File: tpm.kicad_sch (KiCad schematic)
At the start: 3 parts, among them J21 PinHeader_2x7_P2mm_Drill0.9mm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

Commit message: Update naming on schematics, fix OSM page size
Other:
- title: BMC Reference Carrier Board -> DC-SCM Carrier Card for OSM-L SoMs
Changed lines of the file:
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@@
 	(paper "A3")
 	(title_block
-		(title "BMC Reference Carrier Board")
-		(date "2025-10-13")
+		(title "DC-SCM Carrier Card for OSM-L SoMs")
+		(date "2025-10-14")
 		(rev "1.1.0")
 	)

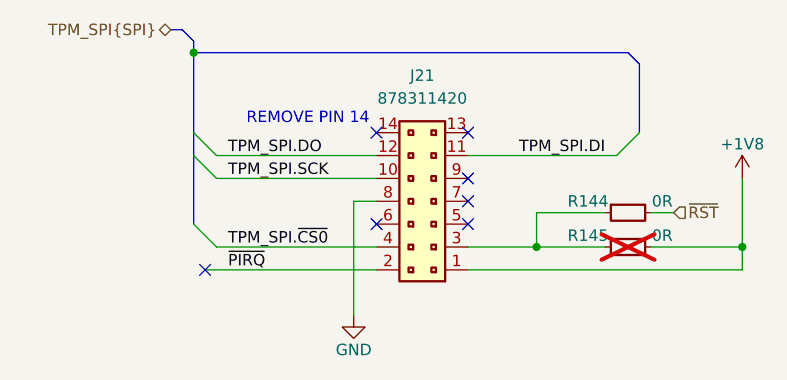
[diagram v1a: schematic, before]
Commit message: Change TPM connector
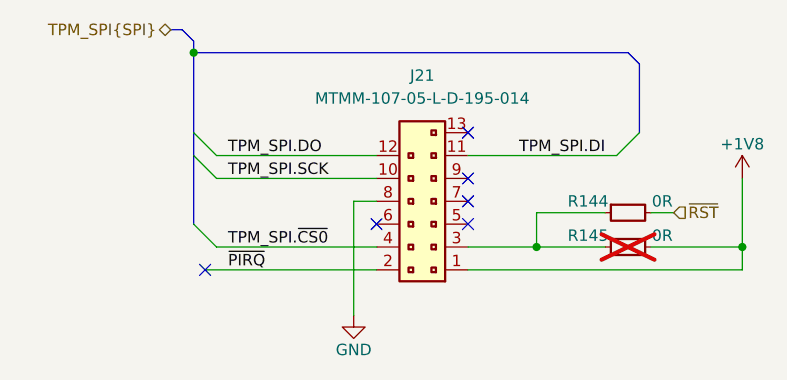
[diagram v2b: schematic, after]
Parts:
- removed J21: PinHeader_2x7_P2mm_Drill0.9mm_878311420, antmicro-footprints:PinHeader_2x7_P2mm_Drill0.9mm_878311420, symbol antmicroGenericPinHeaders:PinHeader_2x7_P2mm_Drill0.9mm_878311420
- added J21: PinHeader_2x7_P2mm_MTMM-107-05-L-D-195-014, antmicro-footprints:PinHeader_2x7_P2mm_Drill0.9mm_MTMM, symbol antmicroGenericPinHeaders:PinHeader_2x7_P2mm_MTMM-107-05-L-D-195-014
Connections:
- net +1V8: now also J21.1
- net GND: now also J21.8
- net TPM_SPI.DI: now also J21.11
- net TPM_SPI.DO: now also J21.12
- net TPM_SPI.SCK: now also J21.10
- net TPM_SPI.~{CS0}: now also J21.4
- net ~{PIRQ}: now also J21.2
- net at R144.1, R145.1: now also J21.3
- no-connect marks 7 -> 6
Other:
- note removed: "REMOVE PIN 14"
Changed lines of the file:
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@@
 		(rev "1.1.0")
-	)
-	(text "REMOVE PIN 14"
-		(exclude_from_sim no)
-		(at 199.39 134.366 0)
-		(effects
-			(font
-				(size 1.27 1.27)
-			)
-		)
 	)
 	(junction
@@
 	(no_connect
 		(at 187.96 151.13)
-	)
-	(no_connect
-		(at 207.01 135.89)
 	)
 	(no_connect
@@
 				)
 				(justify right)
+			)
+		)
+	)
+	(symbol
+		(lib_id "antmicroGenericPinHeaders:PinHeader_2x7_P2mm_MTMM-107-05-L-D-195-014")
+		(at 217.17 151.13 180)
+		(unit 1)
+		(exclude_from_sim no)
+		(in_bom yes)
+		(on_board yes)
+		(dnp no)
+		(fields_autoplaced yes)
+		(property "Reference" "J21"
+			(at 212.09 129.54 0)
+			(effects
+				(font
+					(size 1.27 1.27)
+					(thickness 0.15)
+				)
+			)
+		)
+		(property "Value" "PinHeader_2x7_P2mm_MTMM-107-05-L-D-195-014"
+			(at 191.77 140.97 0)
+			(effects
+				(font
+					(size 1.27 1.27)
+					(thickness 0.15)
+				)
+				(justify left bottom)
+				(hide yes)
+			)
+		)
+		(property "Footprint" "antmicro-footprints:PinHeader_2x7_P2mm_Drill0.9mm_MTMM"
+			(at 191.77 138.43 0)
+			(effects
+				(font
+					(size 1.27 1.27)
+					(thickness 0.15)
+				)
+				(justify left bottom)
+				(hide yes)
+			)
+		)
+		(property "Datasheet" "https://suddendocs.samtec.com/catalog_english/mtmm_th.pdf"
+			(at 191.77 135.89 0)
+			(effects
+				(font
+					(size 1.27 1.27)
+					(thickness 0.15)
+				)
+				(justify left bottom)
+				(hide yes)
+			)
+		)
+		(property "Description" "Pin Header, 2 Rows, 13 Contacts, 2.00mm"
+			(at 191.77 133.35 0)
+			(effects
+				(font
+					(size 1.27 1.27)
+					(thickness 0.15)
+				)
+				(justify left bottom)
+				(hide yes)
+			)
+		)
+		(property "MPN" "MTMM-107-05-L-D-195-014"
+			(at 212.09 132.08 0)
+			(effects
+				(font
+					(size 1.27 1.27)
+					(thickness 0.15)
+				)
+			)
+		)
+		(property "Manufacturer" "Samtec"
+			(at 191.77 130.81 0)
+			(effects
+				(font
+					(size 1.27 1.27)
+					(thickness 0.15)
+				)
+				(justify left bottom)
+				(hide yes)
+			)
+		)
+		(property "Author" "Antmicro"
+			(at 191.77 128.27 0)
+			(effects
+				(font
+					(size 1.27 1.27)
+					(thickness 0.15)
+				)
+				(justify left bottom)
+				(hide yes)
+			)
+		)
+		(property "License" "Apache-2.0"
+			(at 191.77 125.73 0)
+			(effects
+				(font
+					(size 1.27 1.27)
+					(thickness 0.15)
+				)
+				(justify left bottom)
+				(hide yes)
+			)
+		)
+		(pin "9"
+		)
+		(pin "7"
+		)
+		(pin "8"
+		)
+		(pin "2"
+		)
+		(pin "11"
+		)
+		(pin "1"
+		)
+		(pin "3"
+		)
+		(pin "13"
+		)
+		(pin "5"
+		)
+		(pin "12"
+		)
+		(pin "4"
+		)
+		(pin "6"
+		)
+		(pin "10"
+		)
+		(instances
+			(project ""
+				(path "/5f636c45-3c15-4731-8931-4625e0dab7e4/757bd70a-5179-4368-9172-3adb38876975"
+					(reference "J21")
+					(unit 1)
+				)
 			)
 		)
@@
 					(unit 1)
 				)
-			)
-		)
-	)
-	(symbol
-		(lib_id "antmicroGenericPinHeaders:PinHeader_2x7_P2mm_Drill0.9mm_878311420")
-		(at 217.17 151.13 180)
-		(unit 1)
-		(exclude_from_sim no)
-		(in_bom yes)
-		(on_board yes)
-		(dnp no)
-		(fields_autoplaced yes)
-		(property "Reference" "J21"
-			(at 212.09 129.54 0)
-			(effects
-				(font
-					(size 1.27 1.27)
-					(thickness 0.15)
-				)
-			)
-		)
-		(property "Value" "PinHeader_2x7_P2mm_Drill0.9mm_878311420"
-			(at 191.77 146.05 0)
-			(effects
-				(font
-					(size 1.27 1.27)
-					(thickness 0.15)
-				)
-				(justify left bottom)
-				(hide yes)
-			)
-		)
-		(property "Footprint" "antmicro-footprints:PinHeader_2x7_P2mm_Drill0.9mm_878311420"
-			(at 191.77 143.51 0)
-			(effects
-				(font
-					(size 1.27 1.27)
-					(thickness 0.15)
-				)
-				(justify left bottom)
-				(hide yes)
-			)
-		)
-		(property "Datasheet" "https://www.molex.com/en-us/products/part-detail-pdf/878311420?display=pdf"
-			(at 191.77 140.97 0)
-			(effects
-				(font
-					(size 1.27 1.27)
-					(thickness 0.15)
-				)
-				(justify left bottom)
-				(hide yes)
-			)
-		)
-		(property "Description" "2.00mm Pitch, Milli-Grid PCB Header, Dual Row, Vertical, Through Hole, Shrouded, 14 Circuits, 0.38µm Gold (Au) Plating, with Center Polarization Slot, with Locking Window, without PCB Locator, Tube"
-			(at 217.17 151.13 0)
-			(effects
-				(font
-					(size 1.27 1.27)
-				)
-				(hide yes)
-			)
-		)
-		(property "MPN" "878311420"
-			(at 212.09 132.08 0)
-			(effects
-				(font
-					(size 1.27 1.27)
-					(thickness 0.15)
-				)
-			)
-		)
-		(property "Manufacturer" "Molex"
-			(at 191.77 135.89 0)
-			(effects
-				(font
-					(size 1.27 1.27)
-					(thickness 0.15)
-				)
-				(justify left bottom)
-				(hide yes)
-			)
-		)
-		(property "Author" "Antmicro"
-			(at 191.77 133.35 0)
-			(effects
-				(font
-					(size 1.27 1.27)
-					(thickness 0.15)
-				)
-				(justify left bottom)
-				(hide yes)
-			)
-		)
-		(property "License" "Apache-2.0"
-			(at 191.77 130.81 0)
-			(effects
-				(font
-					(size 1.27 1.27)
-					(thickness 0.15)
-				)
-				(justify left bottom)
-				(hide yes)
-			)
-		)
-		(pin "4"
-		)
-		(pin "8"
-		)
-		(pin "13"
-		)
-		(pin "12"
-		)
-		(pin "5"
-		)
-		(pin "14"
-		)
-		(pin "10"
-		)
-		(pin "7"
-		)
-		(pin "9"
-		)
-		(pin "6"
-		)
-		(pin "2"
-		)
-		(pin "3"
-		)
-		(pin "1"
-		)
-		(pin "11"
-		)
-		(instances
-			(project ""
-				(path "/5f636c45-3c15-4731-8931-4625e0dab7e4/757bd70a-5179-4368-9172-3adb38876975"
-					(reference "J21")
-					(unit 1)
-				)
